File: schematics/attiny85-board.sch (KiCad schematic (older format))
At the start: 8 parts, among them SW1 SPST, SW2 SPST

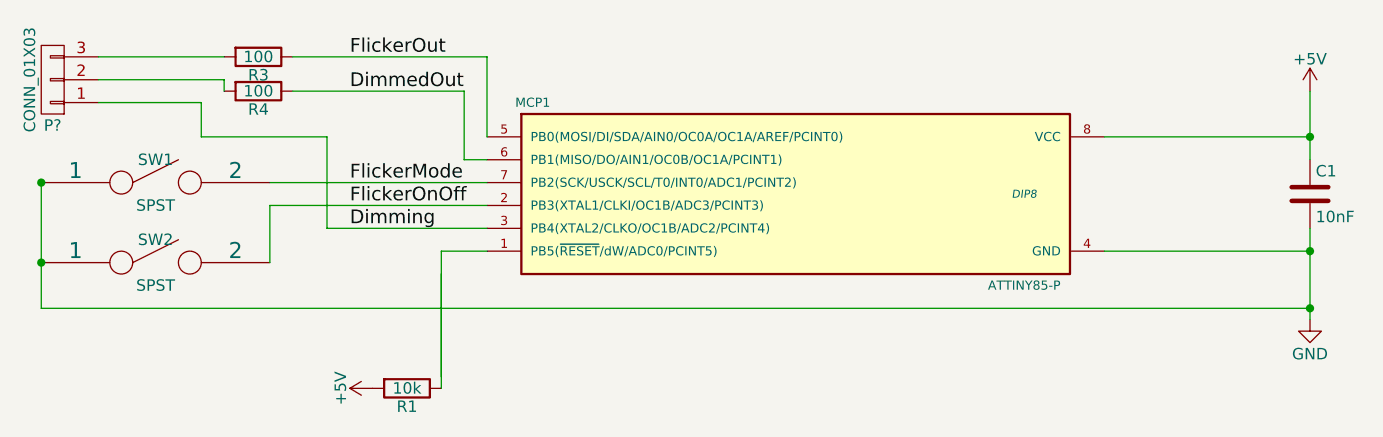
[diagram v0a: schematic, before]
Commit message: Fixed non-connected wire.
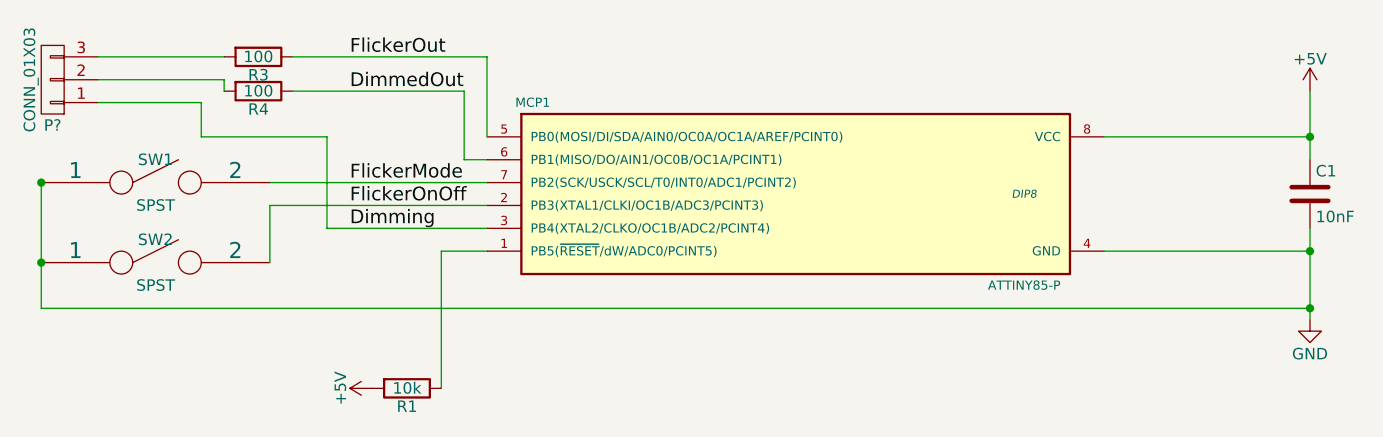
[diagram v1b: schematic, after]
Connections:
- wire segments 30 -> 29
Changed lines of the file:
@@
 Wire Wire Line
 	4850 3850 4850 4450
-Wire Wire Line
-	4850 3950 4850 4400
 $EndSCHEMATC
